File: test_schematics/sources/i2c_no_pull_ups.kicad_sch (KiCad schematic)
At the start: 2 parts, among them U1 PCA9536DP, U2 STM32F030F4Px

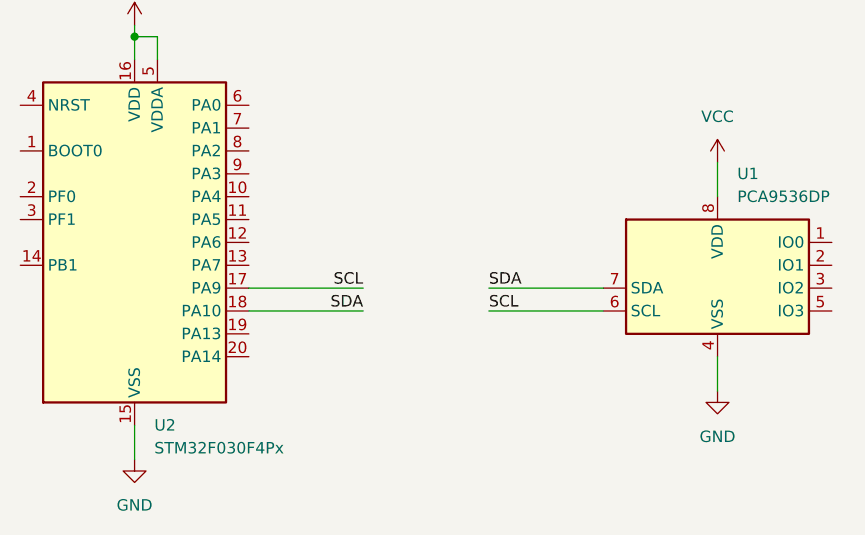
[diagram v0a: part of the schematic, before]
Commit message: refactor: re-annotate test schematics with page X100 designators.
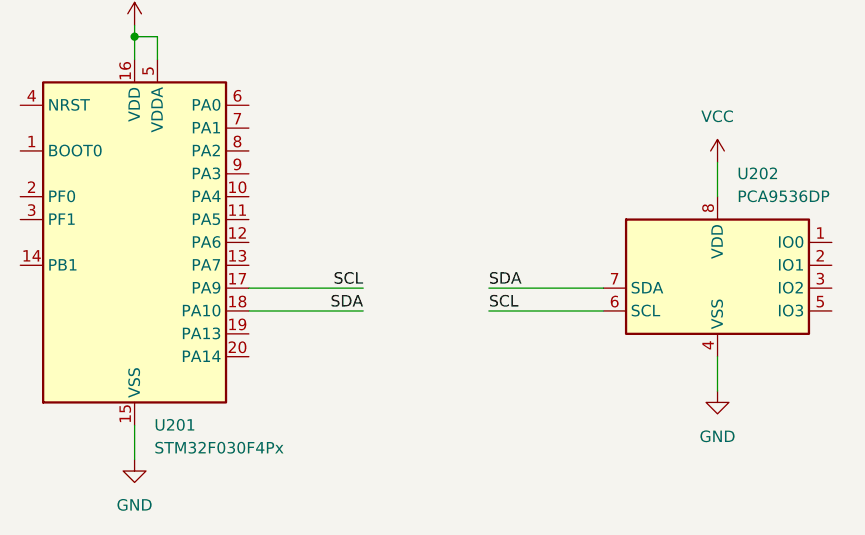
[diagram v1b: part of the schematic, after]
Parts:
- renumbered U2 to U201, U1 to U202
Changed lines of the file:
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@@
 		(dnp no)
 		(fields_autoplaced yes)
-		(property "Reference" "#PWR03"
+		(property "Reference" "#PWR0202"
 			(at 81.28 99.06 0)
 			(effects
@@
 			(project "test_schematics"
 				(path "/f327a4b6-22d9-4671-bd1f-2c46b703509e/29087d8a-217a-4d35-b399-b64f9dad2246"
-					(reference "#PWR03")
+					(reference "#PWR0202")
 					(unit 1)
 				)
@@
 		(dnp no)
 		(fields_autoplaced yes)
-		(property "Reference" "#PWR01"
+		(property "Reference" "#PWR0203"
 			(at 146.05 63.5 0)
 			(effects
@@
 			(project "test_schematics"
 				(path "/f327a4b6-22d9-4671-bd1f-2c46b703509e/29087d8a-217a-4d35-b399-b64f9dad2246"
-					(reference "#PWR01")
+					(reference "#PWR0203")
 					(unit 1)
 				)
@@
 		(dnp no)
 		(fields_autoplaced yes)
-		(property "Reference" "U2"
+		(property "Reference" "U201"
 			(at 83.4741 88.9 0)
 			(effects
@@
 			(project "test_schematics"
 				(path "/f327a4b6-22d9-4671-bd1f-2c46b703509e/29087d8a-217a-4d35-b399-b64f9dad2246"
-					(reference "U2")
+					(reference "U201")
 					(unit 1)
 				)
@@
 		(dnp no)
 		(fields_autoplaced yes)
-		(property "Reference" "U1"
+		(property "Reference" "U202"
 			(at 148.2441 60.96 0)
 			(effects
@@
 			(project "test_schematics"
 				(path "/f327a4b6-22d9-4671-bd1f-2c46b703509e/29087d8a-217a-4d35-b399-b64f9dad2246"
-					(reference "U1")
+					(reference "U202")
 					(unit 1)
 				)
@@
 		(dnp no)
 		(fields_autoplaced yes)
-		(property "Reference" "#PWR04"
+		(property "Reference" "#PWR0201"
 			(at 81.28 48.26 0)
 			(effects
@@
 			(project "test_schematics"
 				(path "/f327a4b6-22d9-4671-bd1f-2c46b703509e/29087d8a-217a-4d35-b399-b64f9dad2246"
-					(reference "#PWR04")
+					(reference "#PWR0201")
 					(unit 1)
 				)
@@
 		(dnp no)
 		(fields_autoplaced yes)
-		(property "Reference" "#PWR02"
+		(property "Reference" "#PWR0204"
 			(at 146.05 91.44 0)
 			(effects
@@
 			(project "test_schematics"
 				(path "/f327a4b6-22d9-4671-bd1f-2c46b703509e/29087d8a-217a-4d35-b399-b64f9dad2246"
-					(reference "#PWR02")
-					(unit 1)
-				)
+					(reference "#PWR0204")
+					(unit 1)
+				)

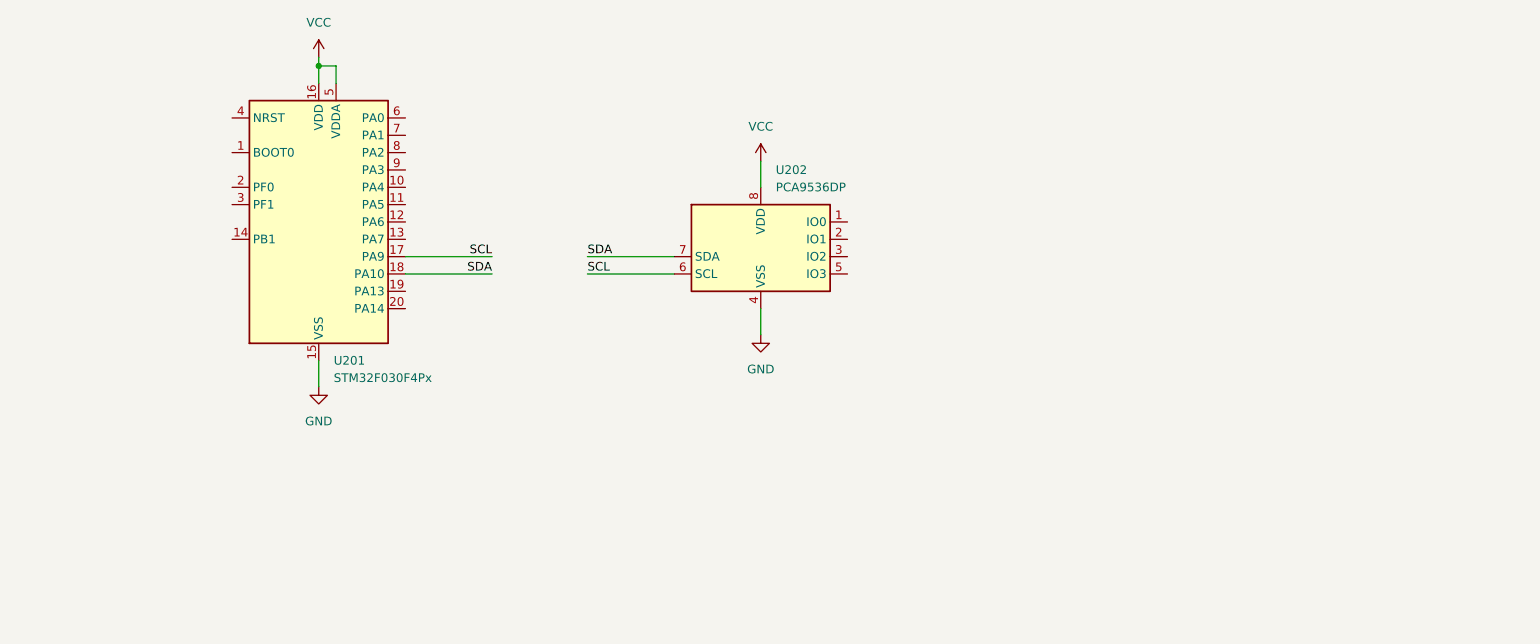
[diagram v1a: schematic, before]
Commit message: feat: identify I2C direct and common segments, check for missing pull-ups or pull-ups to nowhere, identify voltage translators.
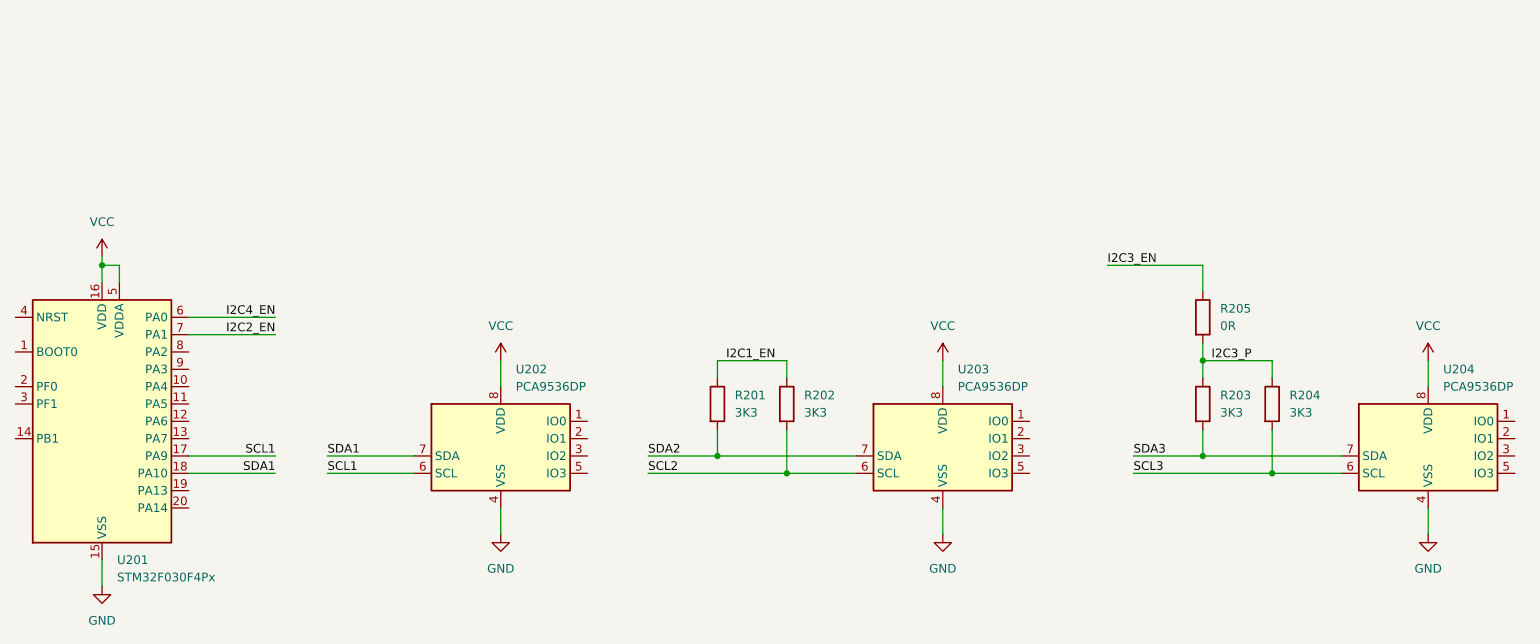
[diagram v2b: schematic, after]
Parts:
- added R201, R202, R203, R204: 3K3, symbol Device:R
- added R205: 0R, symbol Device:R
- added U203, U204: PCA9536DP, Package_SO:TSSOP-8_3x3mm_P0.65mm, symbol Interface_Expansion:PCA9536DP
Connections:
- net GND: now also U203.4 (VSS), U204.4 (VSS)
- net VCC: now also U203.8 (VDD), U204.8 (VDD)
- net I2C4_EN: now reaches U201.6 (PA0)
- net I2C2_EN: now reaches U201.7 (PA1)
- net SCL renamed SCL1
- net SDA renamed SDA1
- new net I2C1_EN: R201.1, R202.1
- new net I2C3_EN: R205.1
- new net I2C3_P: R203.1, R204.1, R205.2
- new net SCL2: R202.2, U203.6 (SCL)
- new net SCL3: R204.2, U204.6 (SCL)
- new net SDA2: R201.2, U203.7 (SDA)
- new net SDA3: R203.2, U204.7 (SDA)
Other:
- moved on the sheet: U201, U202
